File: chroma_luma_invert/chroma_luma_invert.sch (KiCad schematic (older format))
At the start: 36 parts, among them J1 rca, J2 rca, J3 Barrel_Jack, J4 Conn_01x12, SW1 SPDT, SW2 SPDT, U1 AD8044, U3 CD4051, U4 LM317

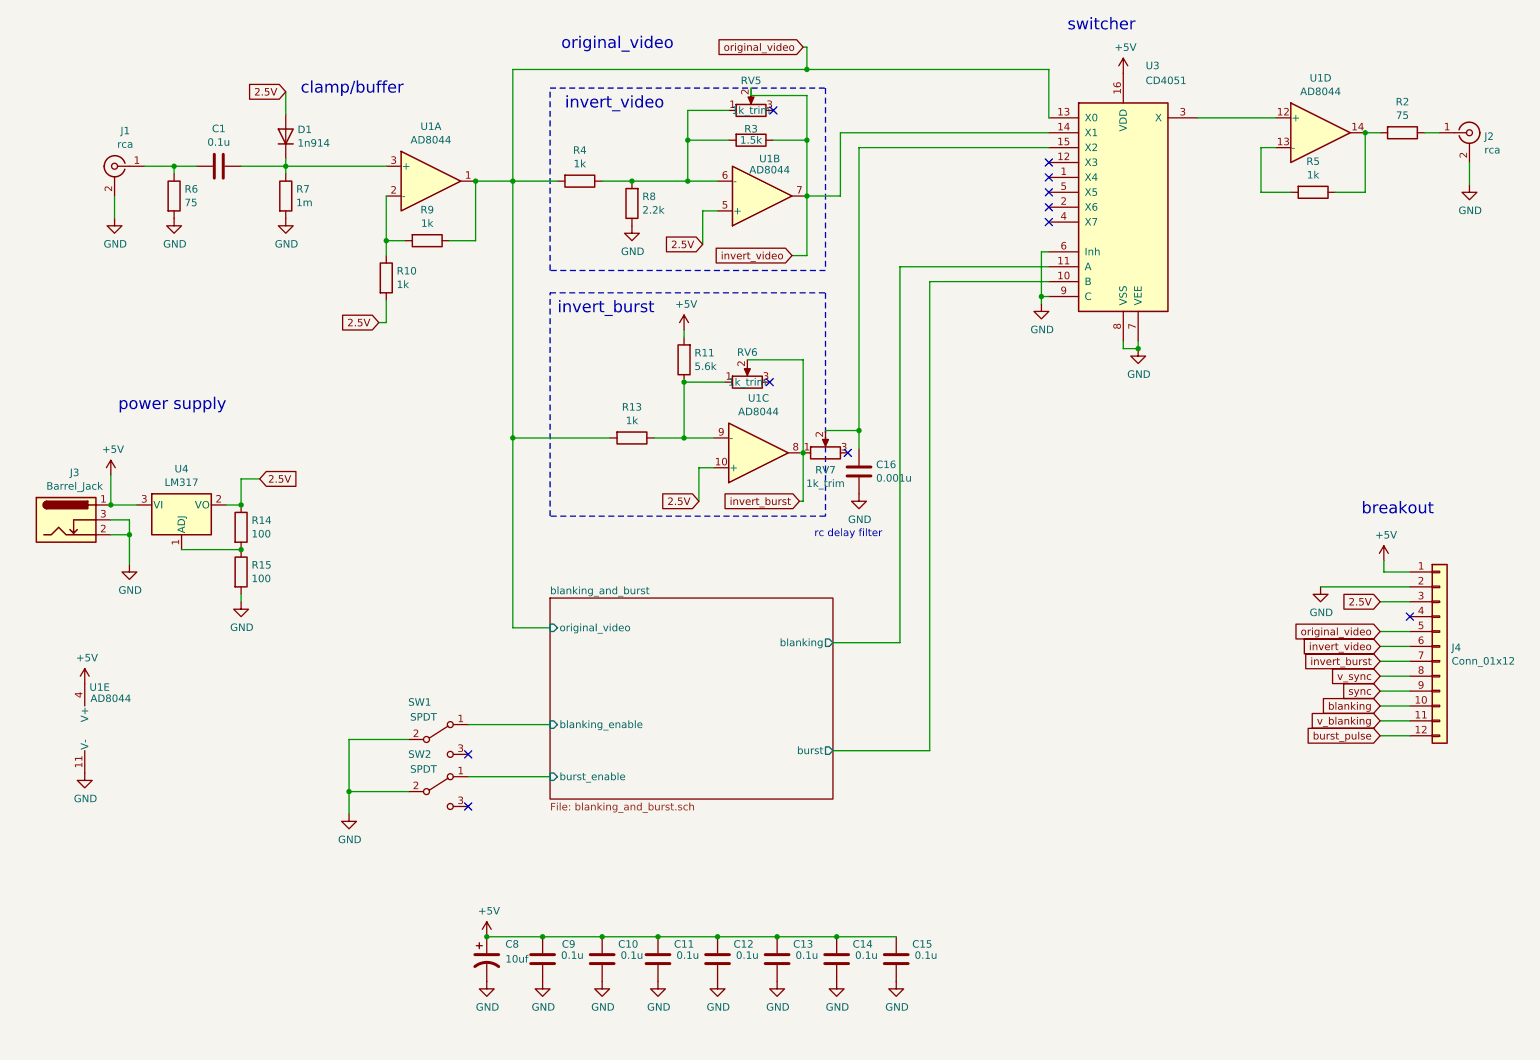
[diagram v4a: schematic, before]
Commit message: update for new chroma_luma circuit
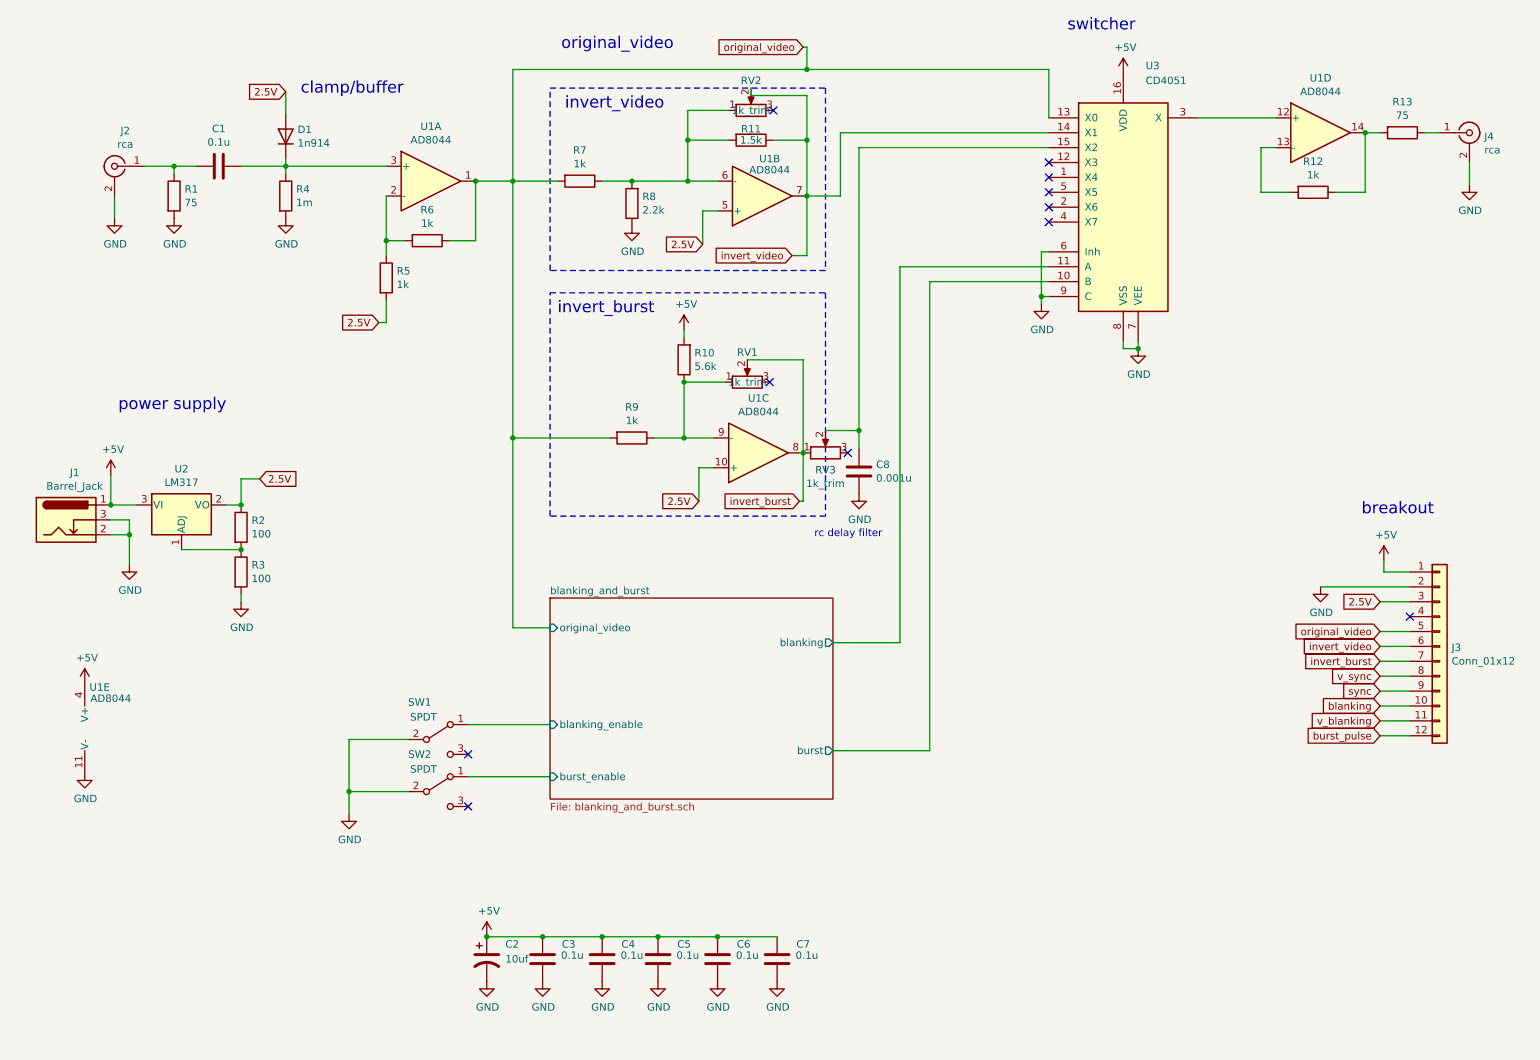
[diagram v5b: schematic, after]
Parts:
- removed C14, C15: 0.1u, Capacitor_THT:C_Disc_D4.7mm_W2.5mm_P5.00mm, symbol Device:C
- U2: renamed from U4; footprint Package_TO_SOT_THT:TO-220-3_Horizontal_TabDown -> Package_TO_SOT_THT:TO-220-3_Vertical
- renumbered C8 to C2, C9 to C3, C10 to C4, C11 to C5, C12 to C6, C13 to C7, C16 to C8, J3 to J1, J1 to J2, J4 to J3, J2 to J4, R6 to R1, R11 to R10, R3 to R11, R5 to R12, R2 to R13, R14 to R2, R15 to R3, R7 to R4, R10 to R5, R9 to R6, R4 to R7, R13 to R9, RV6 to RV1, RV5 to RV2, RV7 to RV3

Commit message: working on nexr version for colorizer and inverter
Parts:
- removed C8: 0.001u, Capacitor_THT:C_Disc_D4.7mm_W2.5mm_P5.00mm, symbol Device:C
- removed R10: 5.6k, Resistor_THT:R_Axial_DIN0207_L6.3mm_D2.5mm_P7.62mm_Horizontal, symbol Device:R
- removed R11: 1.5k, Resistor_THT:R_Axial_DIN0207_L6.3mm_D2.5mm_P7.62mm_Horizontal, symbol Device:R
- removed R7, R9: 1k, Resistor_THT:R_Axial_DIN0207_L6.3mm_D2.5mm_P7.62mm_Horizontal, symbol Device:R
- removed R8: 2.2k, Resistor_THT:R_Axial_DIN0207_L6.3mm_D2.5mm_P7.62mm_Horizontal, symbol Device:R
- removed RV1, RV2, RV3: 1k_trim, lib_fp:tht_vertical_trimpot_3362, symbol Device:R_POT
- removed unit 2 of U1
- removed unit 3 of U1
- SW1, SW2: footprint lib_fp:mini_toggle_switch_tayda -> lib_fp:spdt_slide_switch_small_tayda
- U1: footprint project_parts:DIP+SOIC_14 -> lib_fp:DIP+SOIC_14
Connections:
- net invert_video: no longer U3.14 (X1)
- net invert_logic/invert_burst_output: now reaches U3.15 (X2)
- new net invert_logic/invert_video_output: U3.14 (X1)
- no-connect marks 11 -> 8
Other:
- note removed: "invert_burst"
- note removed: "invert_video"
- note removed: "rc delay filter"
- moved on the sheet: J4, R12, R13, U1D, U3

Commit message: newest circuit revisions
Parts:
- added J5: Conn_02x08_Odd_Even, Connector_PinHeader_2.54mm:PinHeader_2x08_P2.54mm_Vertical, symbol Connector_Generic:Conn_02x08_Odd_Even
- renumbered R12 to R7, R13 to R8
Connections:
- net +5V: now also J5.11 (Pin_11), J5.12 (Pin_12)
- net GND: now also J5.3 (Pin_3), J5.4 (Pin_4), J5.5 (Pin_5), J5.6 (Pin_6), J5.7 (Pin_7), J5.8 (Pin_8)
- no-connect marks 8 -> 16
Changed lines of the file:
@@
 NoConn ~ 7550 1900
 $Comp
-L power:+5V #PWR021
+L power:+5V #PWR018
 U 1 1 5EC0D810
 P 8050 900
-F 0 "#PWR021" H 8050 750 50  0001 C CNN
+F 0 "#PWR018" H 8050 750 50  0001 C CNN
 F 1 "+5V" H 8065 1073 50  0000 C CNN
 F 2 "" H 8050 900 50  0001 C CNN
@@
 $EndComp
 $Comp
-L Device:R R12
+L Device:R R7
 U 1 1 5EC24B54
 P 9300 1700
-F 0 "R12" V 9093 1700 50  0000 C CNN
+F 0 "R7" V 9093 1700 50  0000 C CNN
 F 1 "1k" V 9184 1700 50  0000 C CNN
 F 2 "Resistor_THT:R_Axial_DIN0207_L6.3mm_D2.5mm_P7.62mm_Horizontal" V 9230 1700 50  0001 C CNN
@@
 $EndComp
 $Comp
-L Device:R R13
+L Device:R R8
 U 1 1 5EC26408
 P 9950 1300
-F 0 "R13" V 9743 1300 50  0000 C CNN
+F 0 "R8" V 9743 1300 50  0000 C CNN
 F 1 "75" V 9834 1300 50  0000 C CNN
 F 2 "Resistor_THT:R_Axial_DIN0207_L6.3mm_D2.5mm_P7.62mm_Horizontal" V 9880 1300 50  0001 C CNN
@@
 $EndComp
 $Comp
-L power:GND #PWR025
+L power:GND #PWR022
 U 1 1 5EC28FF2
 P 10450 1650
-F 0 "#PWR025" H 10450 1400 50  0001 C CNN
+F 0 "#PWR022" H 10450 1400 50  0001 C CNN
 F 1 "GND" H 10455 1477 50  0000 C CNN
 F 2 "" H 10450 1650 50  0001 C CNN
@@
 	9975 4475 9775 4475
 $Comp
-L power:+5V #PWR024
+L power:+5V #PWR021
 U 1 1 5ED5EE28
 P 9800 4200
-F 0 "#PWR024" H 9800 4050 50  0001 C CNN
+F 0 "#PWR021" H 9800 4050 50  0001 C CNN
 F 1 "+5V" H 9815 4373 50  0000 C CNN
 F 2 "" H 9800 4200 50  0001 C CNN
@@
 	9800 4275 9800 4200
 $Comp
-L power:GND #PWR023
+L power:GND #PWR020
 U 1 1 5ED61B5B
 P 9375 4375
-F 0 "#PWR023" H 9375 4125 50  0001 C CNN
+F 0 "#PWR020" H 9375 4125 50  0001 C CNN
 F 1 "GND" H 9380 4202 50  0000 C CNN
 F 2 "" H 9375 4375 50  0001 C CNN
@@
 $EndComp
 $Comp
-L power:GND #PWR015
+L power:GND #PWR014
 U 1 1 5F3B3611
 P 4925 7025
-F 0 "#PWR015" H 4925 6775 50  0001 C CNN
+F 0 "#PWR014" H 4925 6775 50  0001 C CNN
 F 1 "GND" H 4930 6852 50  0000 C CNN
 F 2 "" H 4925 7025 50  0001 C CNN
@@
 $EndComp
 $Comp
-L power:GND #PWR017
+L power:GND #PWR015
 U 1 1 5F3B39DD
 P 5325 7025
-F 0 "#PWR017" H 5325 6775 50  0001 C CNN
+F 0 "#PWR015" H 5325 6775 50  0001 C CNN
 F 1 "GND" H 5330 6852 50  0000 C CNN
 F 2 "" H 5325 7025 50  0001 C CNN
@@
 $EndComp
 $Comp
-L power:GND #PWR018
+L power:GND #PWR016
 U 1 1 5F3B3F41
 P 5725 7025
-F 0 "#PWR018" H 5725 6775 50  0001 C CNN
+F 0 "#PWR016" H 5725 6775 50  0001 C CNN
 F 1 "GND" H 5730 6852 50  0000 C CNN
 F 2 "" H 5725 7025 50  0001 C CNN
@@
 	6450 1400 7550 1400
 $Comp
-L power:GND #PWR020
+L power:GND #PWR017
 U 1 1 5EC1216C
 P 7500 2500
-F 0 "#PWR020" H 7500 2250 50  0001 C CNN
+F 0 "#PWR017" H 7500 2250 50  0001 C CNN
 F 1 "GND" H 7505 2327 50  0000 C CNN
 F 2 "" H 7500 2500 50  0001 C CNN
@@
 	7550 1200 7550 900
 $Comp
-L power:GND #PWR014
+L power:GND #PWR019
 U 1 1 61B4819B
 P 8150 2850
-F 0 "#PWR014" H 8150 2600 50  0001 C CNN
+F 0 "#PWR019" H 8150 2600 50  0001 C CNN
 F 1 "GND" H 8155 2677 50  0000 C CNN
 F 2 "" H 8150 2850 50  0001 C CNN
@@
 Wire Wire Line
 	3950 3400 3950 4650
+$Comp
+L Connector_Generic:Conn_02x08_Odd_Even J5
+U 1 1 6167F829
+P 1700 6950
+F 0 "J5" H 1750 6325 50  0000 C CNN
+F 1 "Conn_02x08_Odd_Even" H 1750 6416 50  0000 C CNN
+F 2 "Connector_PinHeader_2.54mm:PinHeader_2x08_P2.54mm_Vertical" H 1700 6950 50  0001 C CNN
+F 3 "~" H 1700 6950 50  0001 C CNN
+	1    1700 6950
+	-1   0    0    1
+$EndComp
+$Comp
+L power:GND #PWR0101
+U 1 1 6168109E
+P 2150 7250
+F 0 "#PWR0101" H 2150 7000 50  0001 C CNN
+F 1 "GND" H 2155 7077 50  0000 C CNN
+F 2 "" H 2150 7250 50  0001 C CNN
+F 3 "" H 2150 7250 50  0001 C CNN
+	1    2150 7250
+	1    0    0    -1
+$EndComp
+Wire Wire Line
+	1900 6950 2150 6950
+Wire Wire Line
+	2150 6950 2150 7050
+Wire Wire Line
+	1900 7150 2150 7150
+Connection ~ 2150 7150
+Wire Wire Line
+	2150 7150 2150 7250
+Wire Wire Line
+	1900 7050 2150 7050
+Connection ~ 2150 7050
+Wire Wire Line
+	2150 7050 2150 7150
+$Comp
+L power:GND #PWR0102
+U 1 1 616890ED
+P 1150 7250
+F 0 "#PWR0102" H 1150 7000 50  0001 C CNN
+F 1 "GND" H 1155 7077 50  0000 C CNN
+F 2 "" H 1150 7250 50  0001 C CNN
+F 3 "" H 1150 7250 50  0001 C CNN
+	1    1150 7250
+	1    0    0    -1
+$EndComp
+Wire Wire Line
+	1150 7250 1150 7150
+Wire Wire Line
+	1150 7150 1400 7150
+Wire Wire Line
+	1150 7150 1150 7050
+Wire Wire Line
+	1150 7050 1400 7050
+Connection ~ 1150 7150
+Wire Wire Line
+	1150 7050 1150 6950
+Wire Wire Line
+	1150 6950 1400 6950
+Connection ~ 1150 7050
+$Comp
+L power:+5V #PWR0103
+U 1 1 616AC00F
+P 1150 6650
+F 0 "#PWR0103" H 1150 6500 50  0001 C CNN
+F 1 "+5V" H 1165 6823 50  0000 C CNN
+F 2 "" H 1150 6650 50  0001 C CNN
+F 3 "" H 1150 6650 50  0001 C CNN
+	1    1150 6650
+	1    0    0    -1
+$EndComp
+Wire Wire Line
+	1150 6750 1400 6750
+Wire Wire Line
+	1150 6650 1150 6750
+$Comp
+L power:+5V #PWR0104
+U 1 1 616B447D
+P 2150 6650
+F 0 "#PWR0104" H 2150 6500 50  0001 C CNN
+F 1 "+5V" H 2165 6823 50  0000 C CNN
+F 2 "" H 2150 6650 50  0001 C CNN
+F 3 "" H 2150 6650 50  0001 C CNN
+	1    2150 6650
+	1    0    0    -1
+$EndComp
+Wire Wire Line
+	2150 6650 2150 6750
+Wire Wire Line
+	2150 6750 1900 6750
+NoConn ~ 1400 6550
+NoConn ~ 1400 6650
+NoConn ~ 1900 6550
+NoConn ~ 1900 6650
+NoConn ~ 1400 6850
+NoConn ~ 1900 6850
+NoConn ~ 1400 7250
+NoConn ~ 1900 7250
 $EndSCHEMATC
